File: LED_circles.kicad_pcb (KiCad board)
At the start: 2 copper layers, 125 x 125 mm, 75 parts, among them J1 Conn_ARM_SWD_TagConnect_TC203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, J2 USB_C_Receptacle_PowerOnly_6P, U3 STM32F070CBTx

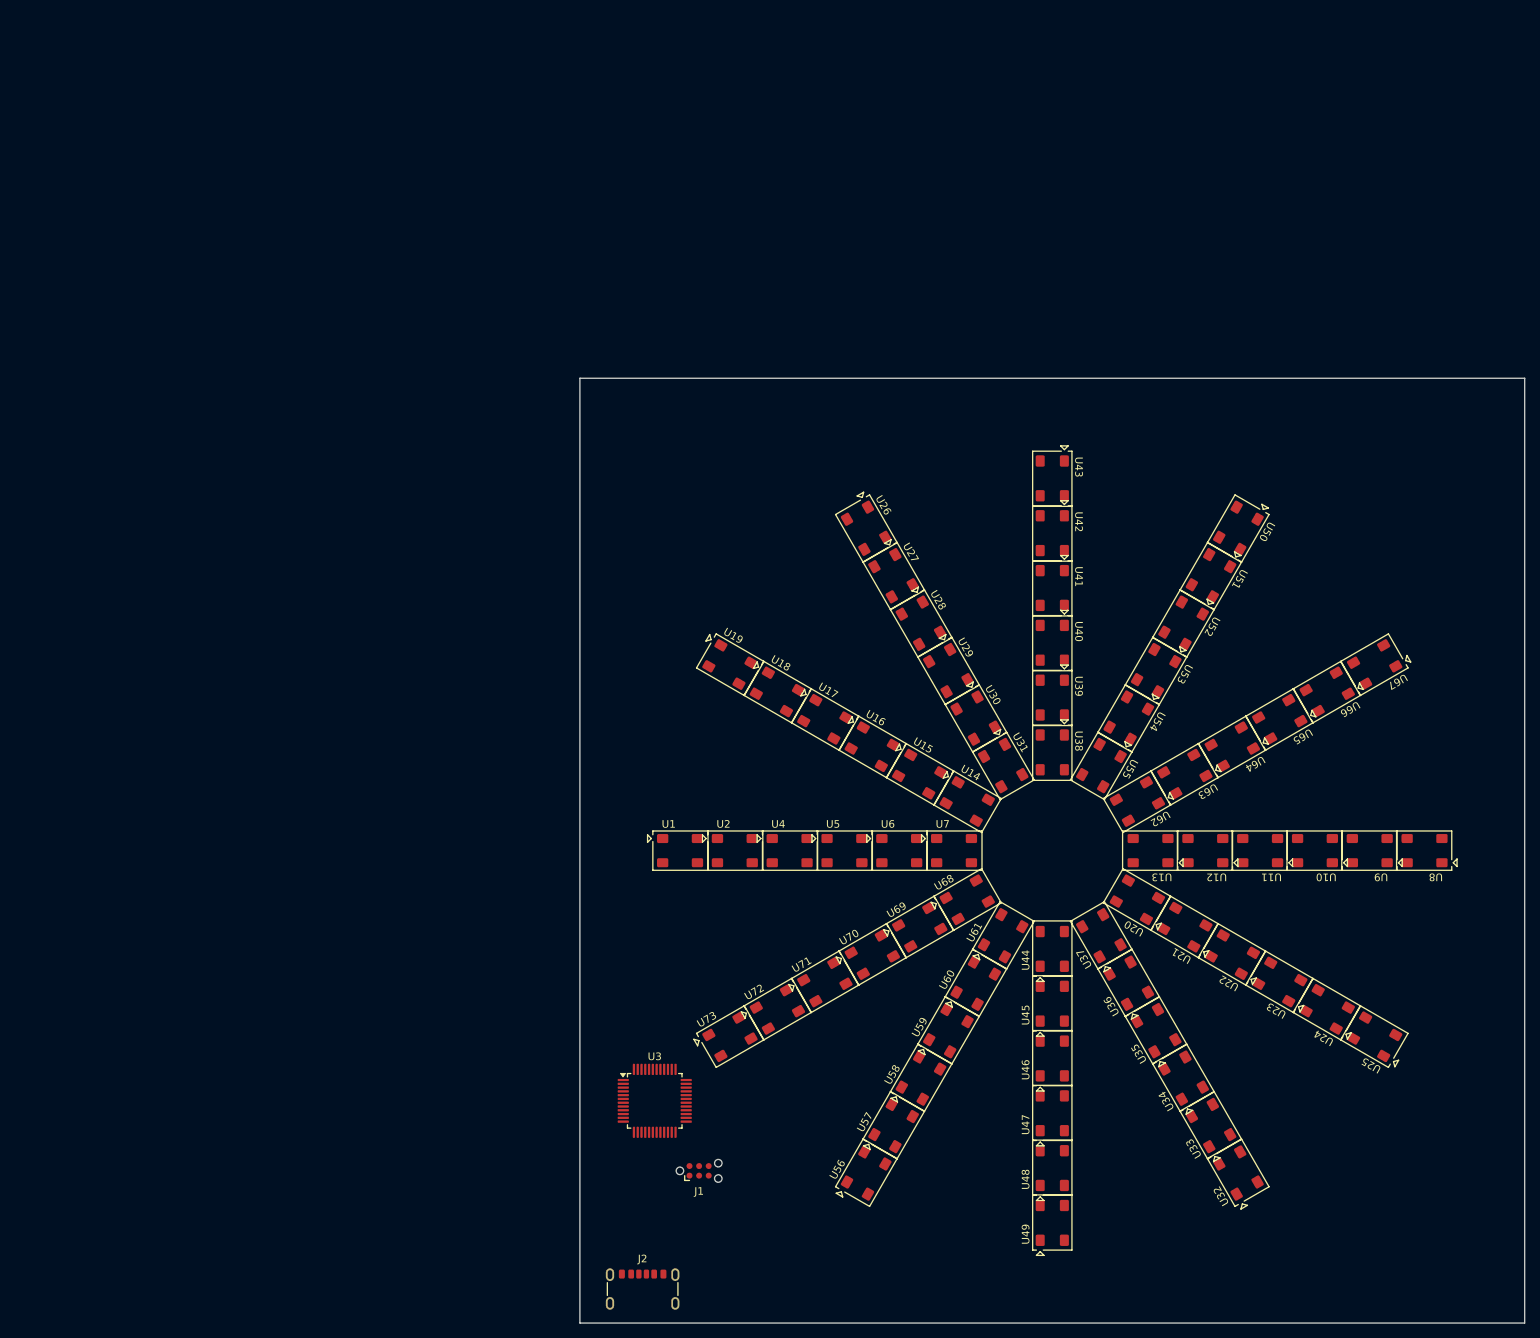
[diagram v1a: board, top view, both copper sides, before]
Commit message: Initial layout of top layer
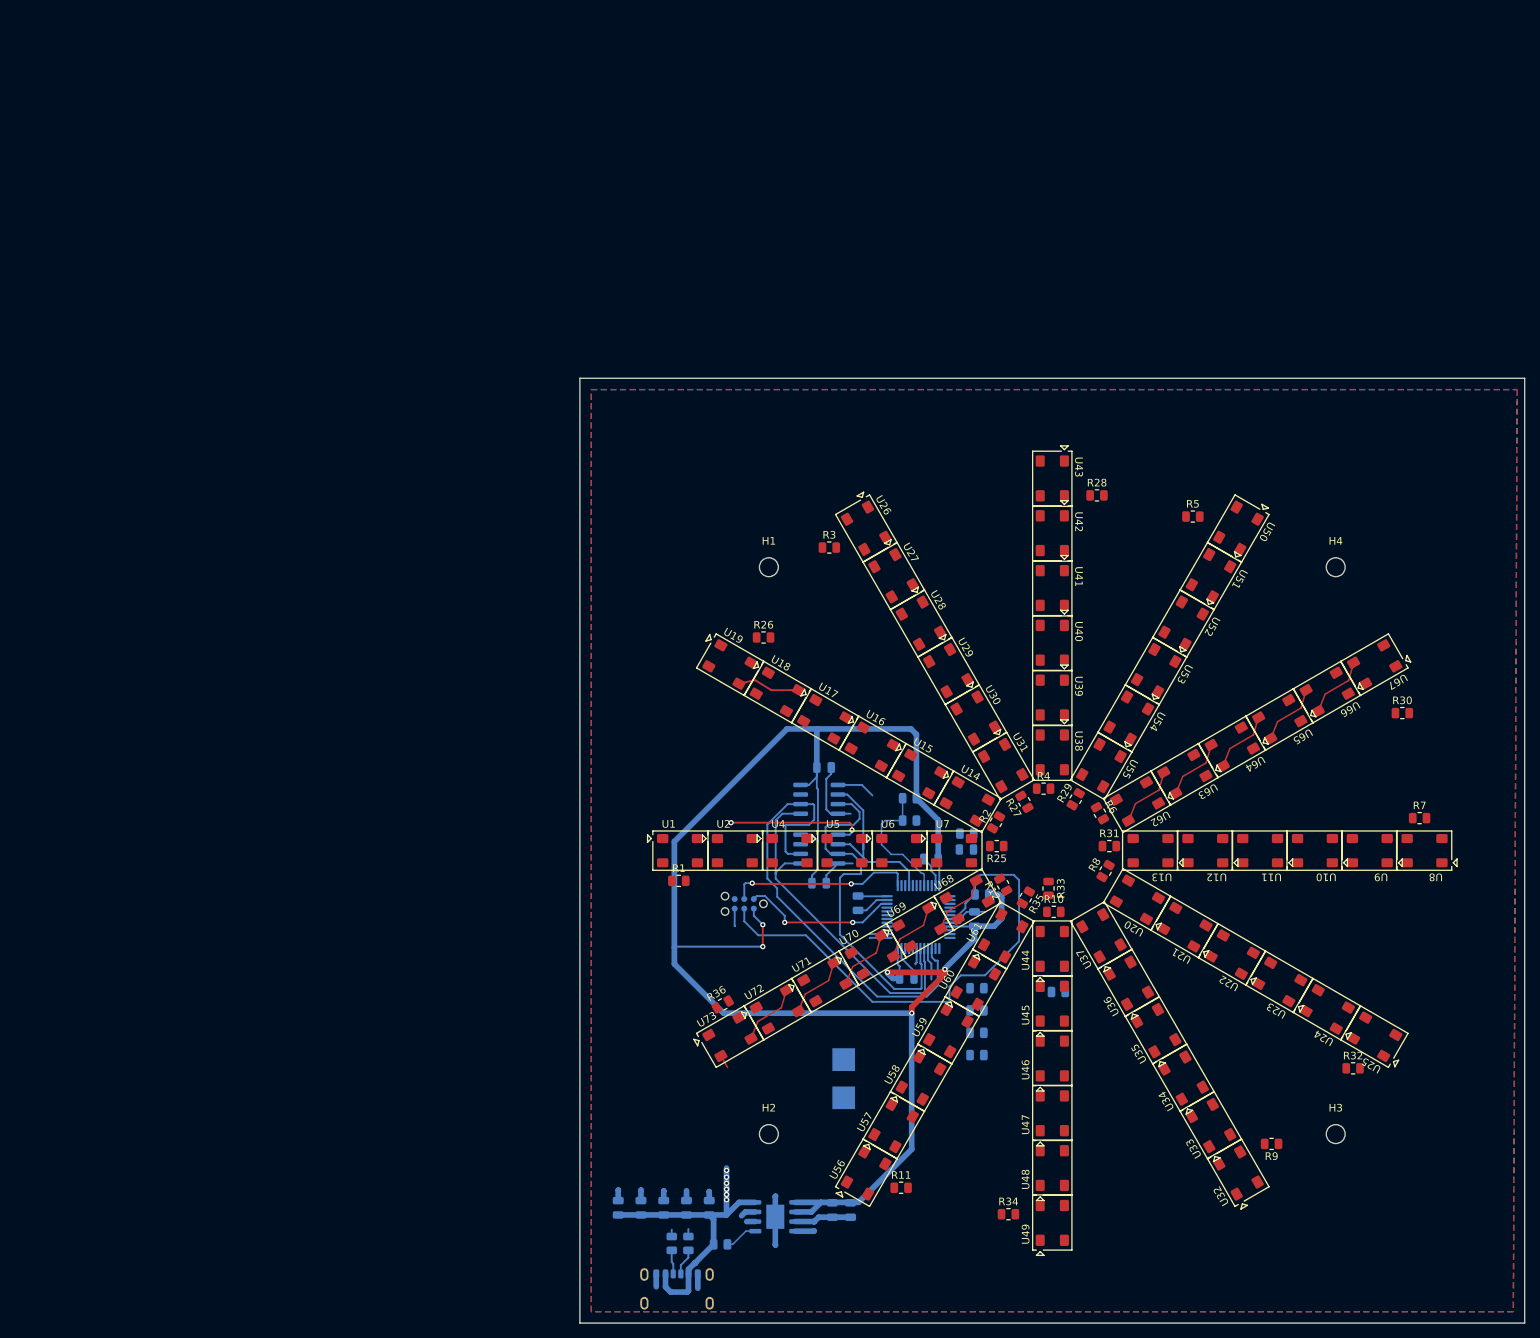
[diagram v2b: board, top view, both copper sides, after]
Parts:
- added C1: 10uF, Capacitor_SMD:C_0805_2012Metric, B.Cu at (98.1, 147.2)
- added C10: .1uF, Capacitor_SMD:C_0805_2012Metric, B.Cu at (124.2, 116.9)
- added C11: .1uF, Capacitor_SMD:C_0805_2012Metric, B.Cu at (127.5, 101.1)
- added C12: .1uF, Capacitor_SMD:C_0805_2012Metric, B.Cu at (113.3, 89.0)
- added C13: .1uF, Capacitor_SMD:C_0805_2012Metric, B.Cu at (112.7, 104.3)
- added C2: 10uF, Capacitor_SMD:C_0805_2012Metric, B.Cu at (95.1, 147.2)
- added C3: 10uF, Capacitor_SMD:C_0805_2012Metric, B.Cu at (92.1, 147.2)
- added C4: 10uF, Capacitor_SMD:C_0805_2012Metric, B.Cu at (89.1, 147.2)
- added C5: 10uF, Capacitor_SMD:C_0805_2012Metric, B.Cu at (86.1, 147.2)
- added C6: 10uF, Capacitor_SMD:C_0805_2012Metric, B.Cu at (114.4, 147.6)
- added C7: 10uF, Capacitor_SMD:C_0805_2012Metric, B.Cu at (116.8, 147.6)
- added C8: .1uF, Capacitor_SMD:C_0805_2012Metric, B.Cu at (117.8, 107.0)
- added C9: .1uF, Capacitor_SMD:C_0805_2012Metric, B.Cu at (133.2, 109.0)
- added D1: LED, LED_SMD:LED_0805_2012Metric, B.Cu at (132.1, 99.8)
- added H1: MountingHole, MountingHole:MountingHole_2.5mm, F.Cu at (106.0, 62.5)
- added H2: MountingHole, MountingHole:MountingHole_2.5mm, F.Cu at (106.0, 137.5)
- added H3: MountingHole, MountingHole:MountingHole_2.5mm, F.Cu at (181.0, 137.5)
- added H4: MountingHole, MountingHole:MountingHole_2.5mm, F.Cu at (181.0, 62.5)
- added R1: 0, Resistor_SMD:R_0805_2012Metric, F.Cu at (94.1, 104.0)
- added R10: 0, Resistor_SMD:R_0805_2012Metric, F.Cu at (143.7, 108.1)
- added R11: 0, Resistor_SMD:R_0805_2012Metric, F.Cu at (123.5, 144.6)
- added R12: 0, Resistor_SMD:R_0805_2012Metric, F.Cu at (137.0, 104.5)
- added R2: 0, Resistor_SMD:R_0805_2012Metric, F.Cu at (136.1, 96.3)
- added R25: 0, Resistor_SMD:R_0805_2012Metric, F.Cu at (136.2, 99.4)
- added R26: 0, Resistor_SMD:R_0805_2012Metric, F.Cu at (105.3, 71.8)
- added R27: 0, Resistor_SMD:R_0805_2012Metric, F.Cu at (139.8, 93.5)
- added R28: 0, Resistor_SMD:R_0805_2012Metric, F.Cu at (149.4, 53.0)
- added R29: 0, Resistor_SMD:R_0805_2012Metric, F.Cu at (146.6, 93.2)
- added R3: 0, Resistor_SMD:R_0805_2012Metric, F.Cu at (114.0, 59.9)
- added R30: 0, Resistor_SMD:R_0805_2012Metric, F.Cu at (189.8, 81.8)
- added R31: 0, Resistor_SMD:R_0805_2012Metric, F.Cu at (151.1, 99.4)
- added R32: 0, Resistor_SMD:R_0805_2012Metric, F.Cu at (183.3, 128.8)
- added R33: 0, Resistor_SMD:R_0805_2012Metric, F.Cu at (143.0, 105.0)
- added R34: 0, Resistor_SMD:R_0805_2012Metric, F.Cu at (137.7, 148.1)
- added R35: 0, Resistor_SMD:R_0805_2012Metric, F.Cu at (140.0, 106.2)
- added R36: 0, Resistor_SMD:R_0805_2012Metric, F.Cu at (99.9, 120.3)
- added R37: 10k, Resistor_SMD:R_0805_2012Metric, B.Cu at (134.2, 105.8)
- added R38: 500, Resistor_SMD:R_0805_2012Metric, B.Cu at (133.5, 118.2)
- added R39: 500, Resistor_SMD:R_0805_2012Metric, B.Cu at (133.5, 121.2)
- added R4: 0, Resistor_SMD:R_0805_2012Metric, F.Cu at (142.3, 91.8)
- added R41: 0, Resistor_SMD:R_0805_2012Metric, B.Cu at (144.3, 118.7)
- added R43: 5k1, Resistor_SMD:R_0805_2012Metric, B.Cu at (93.2, 152.0)
- added R44: 5k1, Resistor_SMD:R_0805_2012Metric, B.Cu at (95.3, 152.0)
- added R45: 0, Resistor_SMD:R_0805_2012Metric, B.Cu at (99.6, 152.1)
- added R46: 10k, Resistor_SMD:R_0805_2012Metric, B.Cu at (133.5, 124.1)
- added R47: 10k, Resistor_SMD:R_0805_2012Metric, B.Cu at (133.5, 127.0)
- added R48: 510, Resistor_SMD:R_0805_2012Metric, B.Cu at (132.2, 97.8)
- added R49: 10k, Resistor_SMD:R_0805_2012Metric, B.Cu at (124.6, 93.1)
- added R5: 0, Resistor_SMD:R_0805_2012Metric, F.Cu at (162.1, 55.8)
- added R50: 10k, Resistor_SMD:R_0805_2012Metric, B.Cu at (124.6, 96.0)
- added R6: 0, Resistor_SMD:R_0805_2012Metric, F.Cu at (149.8, 95.0)
- added R7: 0, Resistor_SMD:R_0805_2012Metric, F.Cu at (192.1, 95.7)
- added R8: 0, Resistor_SMD:R_0805_2012Metric, F.Cu at (150.6, 102.7)
- added R9: 0, Resistor_SMD:R_0805_2012Metric, F.Cu at (172.5, 138.8)
- added TP1: TestPoint, TestPoint:TestPoint_Pad_3.0x3.0mm, B.Cu at (115.9, 127.7)
- added TP2: TestPoint, TestPoint:TestPoint_Pad_3.0x3.0mm, B.Cu at (115.9, 132.7)
- added U74: BD33GA3WEFJ, Package_SO:HTSOP-8-1EP_3.9x4.9mm_P1.27mm_EP2.4x3.2mm, B.Cu at (106.8, 148.4)
- added U75: M95256-WMN6P, Package_SO:SOIC-8_3.9x4.9mm_P1.27mm, B.Cu at (112.7, 93.2)
- added U76: M95256-WMN6P, Package_SO:SOIC-8_3.9x4.9mm_P1.27mm, B.Cu at (112.7, 99.8)
- J1, J2, U3: moved to B.Cu
- moved U3 42.5 mm to (125.8, 108.8), turned to 180 degrees
- moved J1 35.8 mm to (102.7, 107.0), turned to 180 degrees
- moved J2 4.55 mm to (93.8, 159.1), turned to 180 degrees
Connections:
- J1 pad 2: unconnected-(J1-SWDIO-Pad2) -> /LED_circles_ucontroller/SWDIO
- J1 pad 4: unconnected-(J1-SWCLK-Pad4) -> /LED_circles_ucontroller/SWCLK
- J2 pad A12: Net-(J2-GND-PadA12) -> GND
- J2 pad A5: unconnected-(J2-CC1-PadA5) -> Net-(J2-CC1)
- J2 pad A9: Net-(J2-VBUS-PadA9) -> +5V
- J2 pad B12: Net-(J2-GND-PadA12) -> GND
- J2 pad B5: unconnected-(J2-CC2-PadB5) -> Net-(J2-CC2)
- J2 pad B9: Net-(J2-VBUS-PadA9) -> +5V
- J2 pad S1: unconnected-(J2-SHIELD-PadS1) -> GND
- U13 pad 2: Net-(U13-DOUT) -> /Row1/DOUT_{BOTTOM}
- U19 pad 2: Net-(U19-DOUT) -> /Row2/DOUT_{TOP}
- U25 pad 2: Net-(U25-DOUT) -> /Row2/DOUT_{BOTTOM}
- U3 pad 15: unconnected-(U3-PA5-Pad15) -> /LED_circles_ucontroller/SPI1_SCK
- U3 pad 17: unconnected-(U3-PA7-Pad17) -> /LED_circles_ucontroller/SPI1_MOSI
- U3 pad 18: unconnected-(U3-PB0-Pad18) -> /LED_circles_ucontroller/WRITE_PROTECT
- U3 pad 19: unconnected-(U3-PB1-Pad19) -> /LED_circles_ucontroller/HOLD
- U3 pad 25: unconnected-(U3-PB12-Pad25) -> /LED_circles_ucontroller/EEPROM1_CS
- U3 pad 26: unconnected-(U3-PB13-Pad26) -> /LED_circles_ucontroller/EEPROM2_CS
- U3 pad 34: unconnected-(U3-PA13-Pad34) -> /LED_circles_ucontroller/SWDIO
- U3 pad 37: unconnected-(U3-PA14-Pad37) -> /LED_circles_ucontroller/SWCLK
- U3 pad 40: unconnected-(U3-PB4-Pad40) -> /LED_circles_ucontroller/SPI1_MISO
- U3 pad 41: unconnected-(U3-PB5-Pad41) -> Net-(D1-A)
- U3 pad 44: unconnected-(U3-BOOT0-Pad44) -> /LED_circles_ucontroller/BOOT0
- U31 pad 2: Net-(U31-DOUT) -> /Row3/DOUT_{TOP}
- U37 pad 2: Net-(U37-DOUT) -> /Row3/DOUT_{BOTTOM}
- U43 pad 2: Net-(U43-DOUT) -> /Row4/DOUT_{TOP}
- U49 pad 2: Net-(U49-DOUT) -> /Row4/DOUT_{BOTTOM}
- U55 pad 2: Net-(U55-DOUT) -> /Row5/DOUT_{TOP}
- U61 pad 2: Net-(U61-DOUT) -> /Row5/DOUT_{BOTTOM}
- U67 pad 2: Net-(U67-DOUT) -> /Row6/DOUT_{TOP}
- U7 pad 2: Net-(U7-DOUT) -> /Row1/DOUT_{TOP}
- U73 pad 2: Net-(U73-DOUT) -> /Row6/DOUT_{BOTTOM}
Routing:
- net +3.3V: track 0.00 -> 239.4 mm, vias 0 -> 5
- net Net-(J1-~{RESET}): track 0.00 -> 68.6 mm
- net GND: track 0.00 -> 67.4 mm
- net /LED_circles_ucontroller/SPI1_SCK: track 0.00 -> 61.9 mm
- net /LED_circles_ucontroller/WRITE_PROTECT: track 0.00 -> 48.6 mm
- net /LED_circles_ucontroller/SPI1_MOSI: track 0.00 -> 47.2 mm
- net +5V: track 0.00 -> 43.6 mm, vias 0 -> 6
- net /LED_circles_ucontroller/SWCLK: track 0.00 -> 24.6 mm, vias 0 -> 2
- net /LED_circles_ucontroller/SPI1_MISO: track 0.00 -> 23.9 mm
- net /LED_circles_ucontroller/EEPROM1_CS: track 0.00 -> 21.4 mm, vias 0 -> 2
- net /LED_circles_ucontroller/SWDIO: track 0.00 -> 21.0 mm, vias 0 -> 2
- net /LED_circles_ucontroller/BOOT0: track 0.00 -> 17.4 mm
- net Net-(U68-DOUT): track 0.00 -> 8.45 mm
- net Net-(U71-DOUT): track 0.00 -> 8.45 mm
- net Net-(U66-DOUT): track 0.00 -> 8.45 mm
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- added copper zone on F.Cu, net +5V
- added copper zone on B.Cu, net GND

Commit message: Inital layout
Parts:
- added C14: .1uF, Capacitor_SMD:C_0805_2012Metric, B.Cu at (132.8, 99.5)
- added R13: 0, Resistor_SMD:R_0805_2012Metric, F.Cu at (188.0, 91.0)
- R41: moved to F.Cu
- moved D1 58.5 mm to (122.3, 157.6)
- moved R48 58.5 mm to (122.4, 155.4)
- moved R41 55.7 mm to (192.6, 91.0), turned to 0 degrees
- moved R47 51.7 mm to (122.2, 76.6), turned to -90 degrees
- moved R46 49.8 mm to (118.5, 76.6), turned to -90 degrees
- moved TP1 32.5 mm to (130.0, 156.9), turned to -90 degrees
- moved TP2 30.9 mm to (135.1, 156.9), turned to -90 degrees
- moved R39 18.6 mm to (115.2, 124.2)
- moved C13 12.6 mm to (112.7, 91.7)
- moved C12 12.0 mm to (113.3, 77.0)
- moved U76 12.0 mm to (112.7, 87.8)
- moved U75 11.9 mm to (112.7, 81.3)
- moved R33 3.99 mm to (146.8, 104.0)
- moved R29 3.37 mm to (145.7, 96.4)
- moved R30 3.28 mm to (187.1, 79.9), turned to -150 degrees
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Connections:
- net Net-(U3-PA10) renamed /LED_circles_ucontroller/RX
- net Net-(U3-PA9) renamed /LED_circles_ucontroller/TX
- R41 pad 1: /LED_circles_ucontroller/BOTTOM_ROWS -> /Row1/DIN_{BOTTOM}
- R7 pad 1: /LED_circles_ucontroller/BOTTOM_ROWS -> /Row1/DIN_{BOTTOM}
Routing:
- net GND: track 67.4 -> 223.4 mm, vias 0 -> 73
- net +5V: track 43.6 -> 178.2 mm, vias 6 -> 7
- net Net-(D1-A): track 0.00 -> 128.7 mm, vias 0 -> 10
- net /LED_circles_ucontroller/TX: track 0.00 -> 90.9 mm, vias 0 -> 3
- net /LED_circles_ucontroller/RX: track 0.00 -> 87.7 mm, vias 0 -> 3
- net /LED_circles_ucontroller/HOLD: track 2.16 -> 89.5 mm, vias 0 -> 6
- net +3.3V: track 239.4 -> 321.1 mm, vias 5 -> 8
- net /LED_circles_ucontroller/BOTTOM_ROWS: track 0.00 -> 65.7 mm, vias 0 -> 1
- net /LED_circles_ucontroller/EEPROM2_CS: track 7.42 -> 60.8 mm, vias 0 -> 2
- net /LED_circles_ucontroller/EEPROM1_CS: track 21.4 -> 63.4 mm, vias 2 -> 3
- net /LED_circles_ucontroller/TOP_ROWS: track 0.00 -> 33.3 mm, vias 0 -> 1
- net /Row2/DOUT_{TOP}: track 0.00 -> 21.3 mm, vias 0 -> 2
- net /Row4/DOUT_{TOP}: track 0.00 -> 20.3 mm, vias 0 -> 2
- net Net-(U3-PA8): track 0.00 -> 19.7 mm, vias 0 -> 4
- net /Row4/DOUT_{BOTTOM}: track 0.00 -> 19.6 mm
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
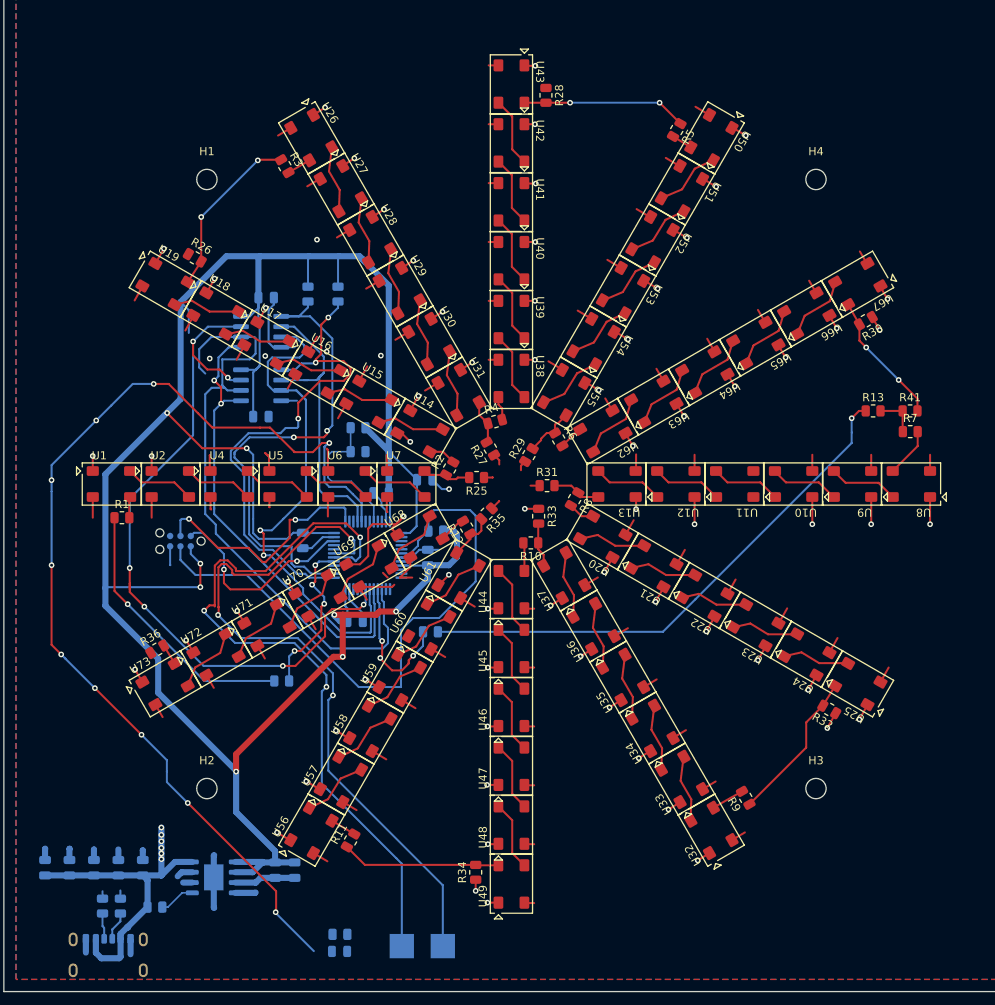
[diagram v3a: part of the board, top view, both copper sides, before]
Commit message: Added all connections to PCB
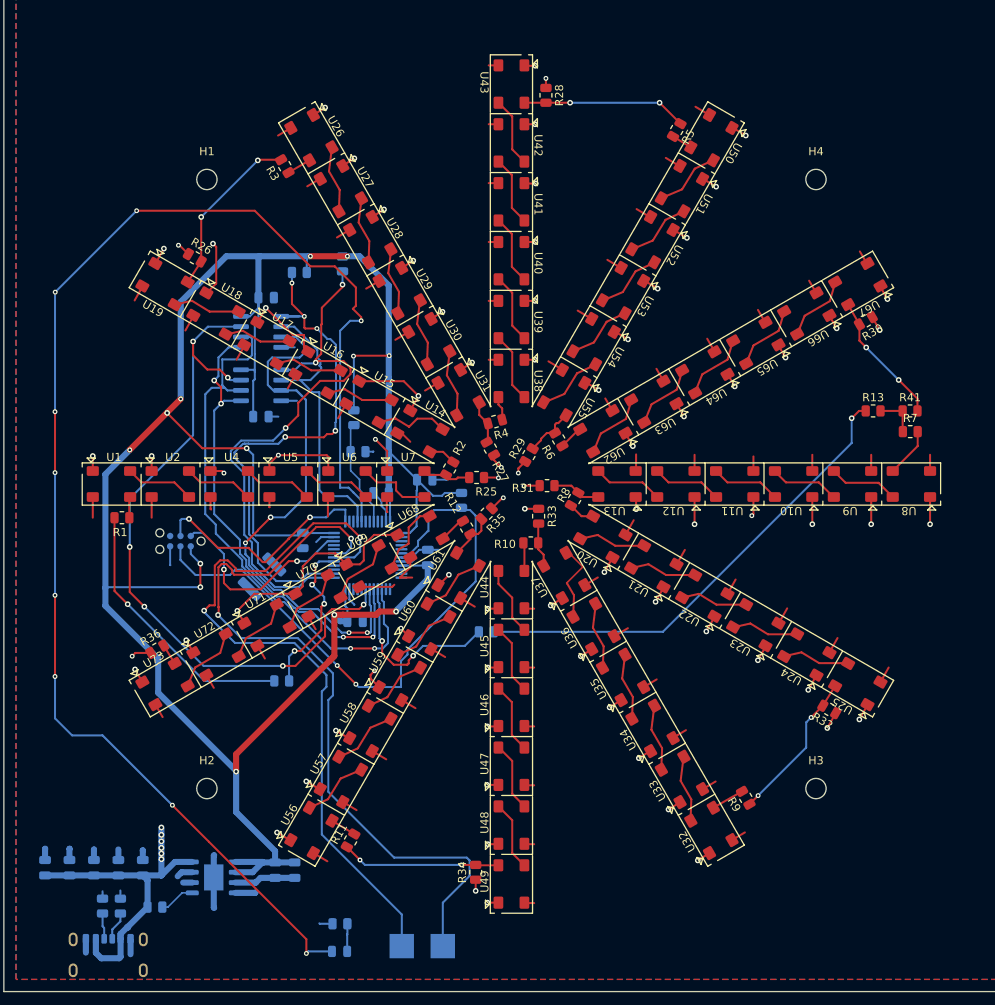
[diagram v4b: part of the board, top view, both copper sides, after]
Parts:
- added R14: 0, Resistor_SMD:R_1812_4532Metric, B.Cu at (112.8, 111.4)
- moved R38 6.87 mm to (140.4, 118.2)
- moved R37 4.93 mm to (137.3, 102.0), turned to -90 degrees
- moved R47 3.75 mm to (122.7, 72.9)
- moved R46 2.87 mm to (117.4, 74.0), turned to 180 degrees
- moved R49 1.33 mm to (124.1, 91.8), turned to -90 degrees
- moved R48 1.30 mm to (122.4, 154.2)
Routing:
- net Net-(D1-A): track 128.7 -> 177.8 mm, vias 10 -> 9
- net GND: track 223.4 -> 262.7 mm, vias 73 -> 78
- net /LED_circles_ucontroller/SPI1_SCK: track 77.7 -> 68.3 mm, vias 0 -> 2
- net /LED_circles_ucontroller/BOTTOM_ROWS: track 65.7 -> 58.9 mm
- net /LED_circles_ucontroller/RX: track 87.7 -> 94.5 mm, vias 3 -> 2
- net /LED_circles_ucontroller/EEPROM2_CS: track 60.8 -> 66.9 mm, vias 2 -> 5
- net /LED_circles_ucontroller/EEPROM1_CS: track 63.4 -> 69.0 mm
- net +3.3V: track 321.1 -> 315.6 mm, vias 8 -> 13
- net /LED_circles_ucontroller/BOOT0: track 17.8 -> 12.7 mm
- net Net-(U3-PA6): track 17.9 -> 22.5 mm, vias 3 -> 2
- net Net-(D1-K): track 0.00 -> 3.41 mm
- net /LED_circles_ucontroller/WRITE_PROTECT: track 64.6 -> 67.6 mm, vias 2 -> 4
- net Net-(U36-DOUT): track 8.26 -> 10.0 mm
- net /LED_circles_ucontroller/SWCLK: track 30.3 -> 28.7 mm
- net Net-(J1-~{RESET}): track 75.7 -> 74.3 mm, vias 0 -> 2
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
